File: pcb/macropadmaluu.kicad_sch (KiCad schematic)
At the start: 9 parts, among them SW1 SW_Push, SW2 SW_Push, SW3 SW_Push, SW4 SW_Push, SW5 SW_Push, SW6 SW_Push, U1 XIAO-RP2040-DIP

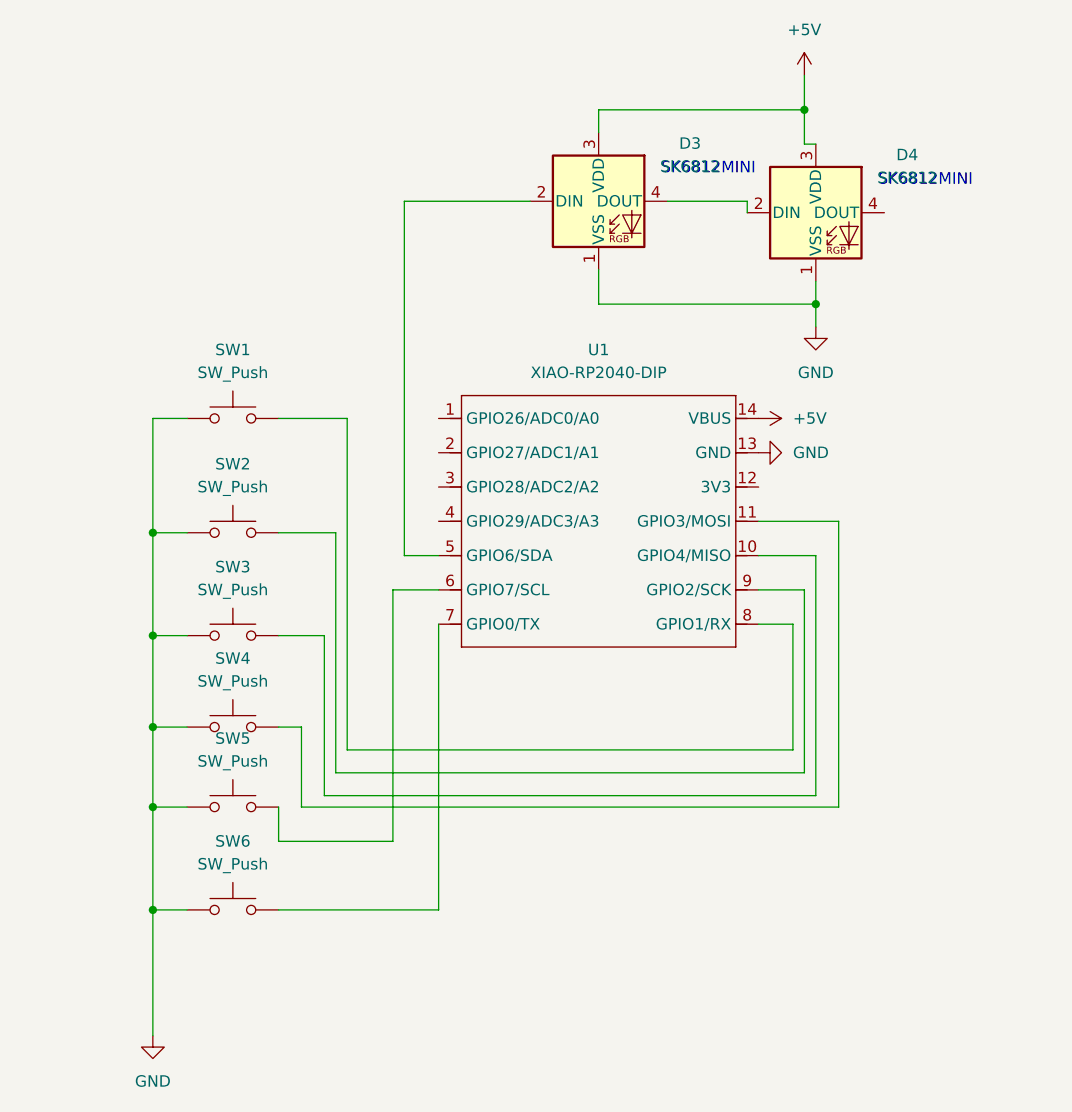
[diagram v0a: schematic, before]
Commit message: Add Gerber and drill files for macropadmaluu project
- Created non-plated through-hole (NPTH) drill file: macropadmaluu-NPTH.drl
- Created plated through-hole (PTH) drill file: macropadmaluu-PTH.drl
- Added job file for Gerber generation: macropadmaluu-job.gbrjob
- All files generated using KiCad version 9.0.6 with appropriate specifications and attributes.
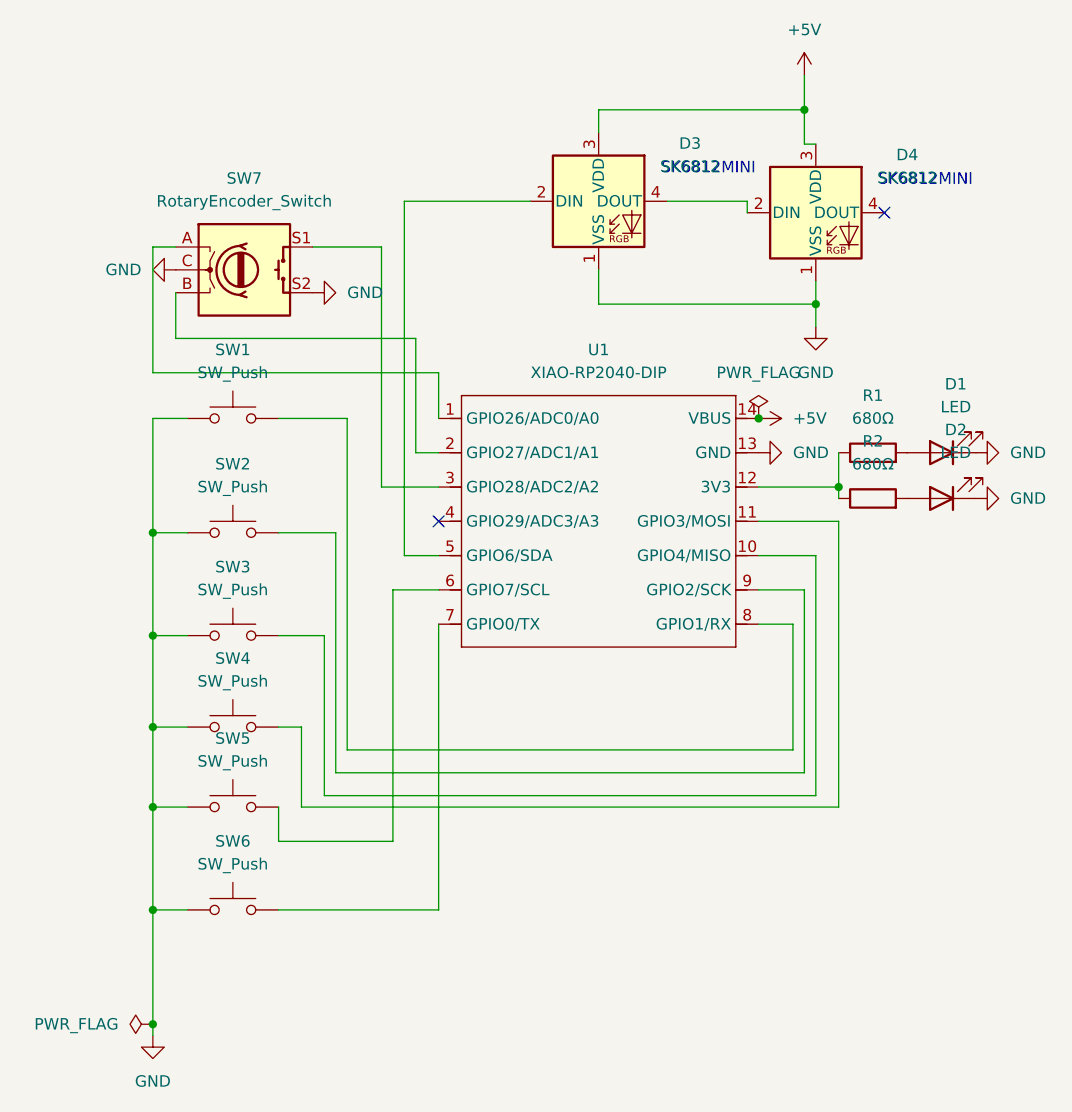
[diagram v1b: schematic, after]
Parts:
- added D1, D2: LED, LED_THT:LED_D3.0mm, symbol Device:LED
- added R1, R2: 680Ω, Resistor_THT:R_Axial_DIN0207_L6.3mm_D2.5mm_P7.62mm_Horizontal, symbol Device:R
- added SW7: RotaryEncoder_Switch, Rotary_Encoder:RotaryEncoder_Alps_EC11E-Switch_Vertical_H20mm, symbol Device:RotaryEncoder_Switch
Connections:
- net GND: now also D1.1 (K), D2.1 (K), SW7.C, SW7.S2
- net at U1.1 (GPIO26/ADC0/A0): now also SW7.A
- net at U1.12 (3V3): now also R1.1, R2.1
- net at U1.2 (GPIO27/ADC1/A1): now also SW7.B
- net at U1.3 (GPIO28/ADC2/A2): now also SW7.S1
- new net: D2.2 (A), R2.2
- new net: D1.2 (A), R1.2
- no-connect marks 0 -> 2
